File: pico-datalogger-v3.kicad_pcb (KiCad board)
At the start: 2 copper layers, 130 x 65 mm, 60 parts, among them IC1 LM66200DRLR, J1 JST-PH2 Bat, J11 Conn_I2C1, J12 Conn_UART_5V, J13 THT_I2C1, J14 THT_I2C0, J17 Disp_THT, J2 Conn_Pico_Left, J3 Conn_Pico_Right, J4 SM06B-GHS-TB_LF_SN, J6 Conn_Display, J9 Conn_I2C0, Q1 AO3401A, Q2 AO3401A, SW1 SW_Push, SW2 SW_Push, SW3 SW_Push, SW4 SW_Push, SW5 SW_Push, U1 74LVC2G74, U2 PCF8523T, U4 XTSD, U5 SCD40_Breakout, U6 AHT20, U7 RFM95W-868S2, Y1 Crystal

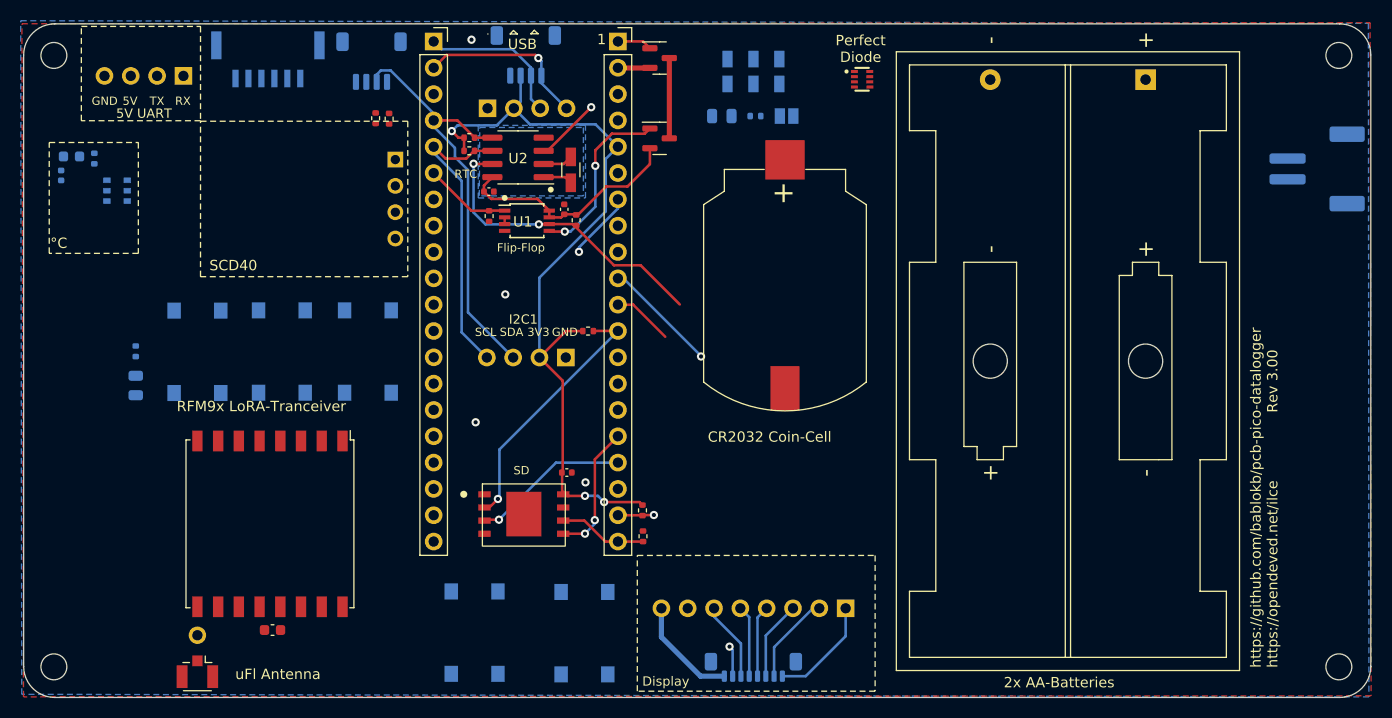
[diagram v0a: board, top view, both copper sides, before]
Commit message: move AA-holder away from mounting-hole
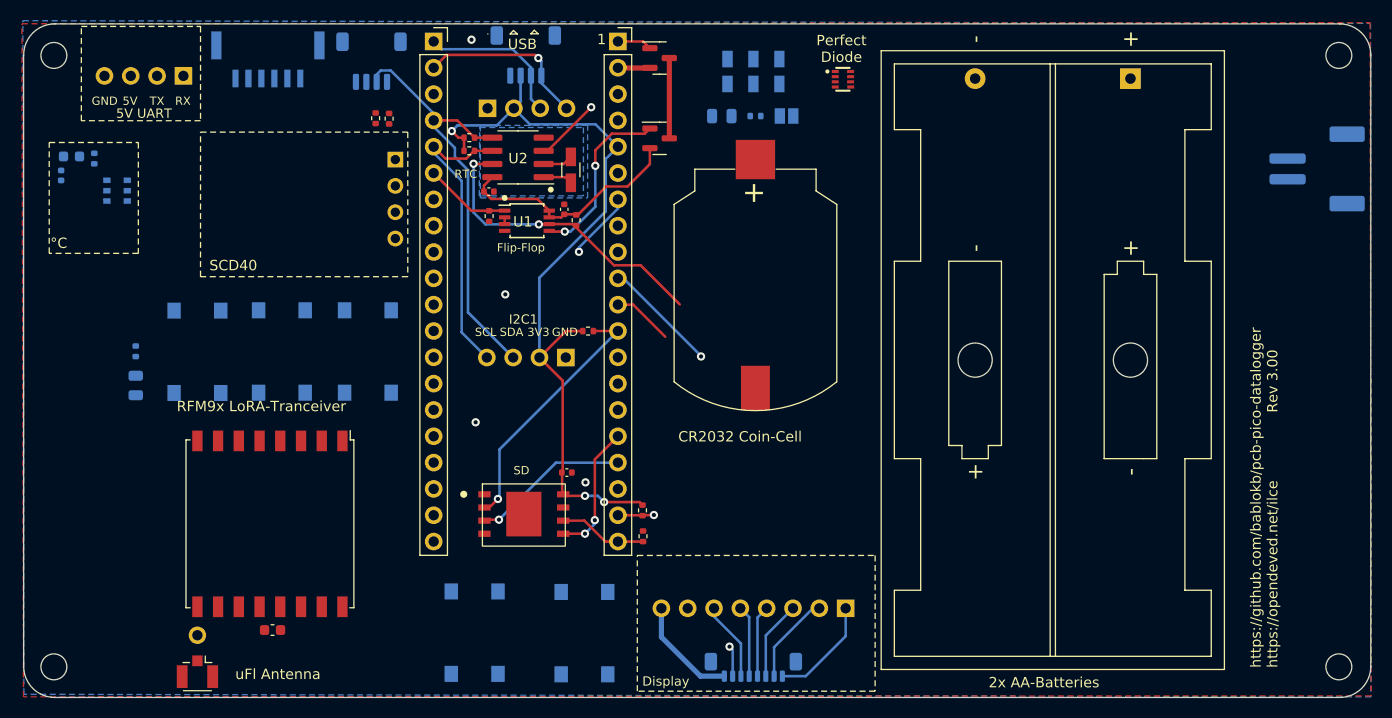
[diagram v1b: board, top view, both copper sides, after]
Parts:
- moved BT1 2.85 mm to (170.7, 124.1)
- moved G*** 2.37 mm to (197.1, 136.0)
- moved IC1 1.85 mm to (179.1, 105.3)
- moved BT2 1.46 mm to (206.9, 105.2)
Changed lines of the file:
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@@
   )
   (footprint "user:LM66200DRLR" (layer "F.Cu")
-    (at 180.99 105.3 -90)
+    (at 179.14 105.3 -90)
     (descr "LM66200DRLR Perfect Diode")
     (property "Description" "1.6-V to 5.5-V, 40-mΩ, 2.5-A, low-IQ, dual ideal diode")
@@
   )
   (footprint "Battery:BatteryHolder_Keystone_2462_2xAA" (layer "F.Cu")
-    (at 208.35 105.335 -90)
+    (at 206.89 105.235 -90)
     (descr "2xAA cell battery holder, Keystone P/N 2462, https://www.keyelco.com/product-pdf.cfm?p=1027")
     (tags "AA battery cell holder")
@@
   )
   (footprint "user:CR2032_Holder" (layer "F.Cu")
-    (at 173.55 124.1 90)
+    (at 170.7 124.075 90)
     (descr "Coin-Cell CR2032")
     (property "LCSC" "C964777")
@@
   )
   (footprint "user:giraffe" locked (layer "B.Cu")
-    (at 199.45 136 180)
+    (at 197.082707 135.960722 180)
     (attr board_only exclude_from_pos_files exclude_from_bom)
     (fp_text reference "G***" (at 0 0) (layer "B.SilkS")
@@
     )
   )
-  (gr_rect (start 105.65 109.3) (end 117.15 100.2)
+  (gr_rect (start 105.65 100.2) (end 117.15 109.3)
     (stroke (width 0.12) (type dash)) (fill none) (layer "B.SilkS"))
   (gr_rect (start 102.55 111.4) (end 111.15 122.05)
@@
   (gr_rect (start 165.105 100.4) (end 175.955 112.05)
     (stroke (width 0.12) (type default)) (fill none) (layer "B.SilkS"))
-  (gr_rect (start 184.15 102.4) (end 217.65 162.45)
+  (gr_rect (start 182.8 102.325) (end 216.3 162.375)
     (stroke (width 0.2) (type dash)) (fill none) (layer "B.SilkS"))
-  (gr_rect (start 158.85 150.75) (end 182.8 164.35)
+  (gr_rect (start 158.85 150.75) (end 182.3 164.35)
     (stroke (width 0.12) (type solid)) (fill none) (layer "B.SilkS"))
   (gr_rect (start 105.65 100.2) (end 117.15 109.3)
@@
   (gr_line (start 147.02 100.93) (end 147.35 100.59)
     (stroke (width 0.12) (type solid)) (layer "F.SilkS"))
-  (gr_rect (start 117.15 109.35) (end 137.15 124.35)
+  (gr_rect (start 117.15 110.4) (end 137.15 124.35)
     (stroke (width 0.12) (type dash)) (fill none) (layer "F.SilkS"))
   (gr_line (start 144.89 100.93) (end 144.87 100.93)
@@
     (effects (font (size 1 1) (thickness 0.15)) (justify left bottom mirror))
   )
-  (gr_text "Display" (at 180.25 163.4) (layer "B.SilkS")
+  (gr_text "Display" (at 179.65 163.35) (layer "B.SilkS")
     (effects (font (size 0.9 0.9) (thickness 0.15)) (justify mirror))
   )
@@
     (effects (font (size 0.8 0.8) (thickness 0.15)) (justify mirror))
   )
-  (gr_text "2x AA-Batteries" (at 207 161.2) (layer "B.SilkS")
+  (gr_text "2x AA-Batteries" (at 205.59143 161.2) (layer "B.SilkS")
     (effects (font (size 1 1) (thickness 0.15)) (justify left bottom mirror))
   )
@@
     (effects (font (size 0.8 0.8) (thickness 0.15)))
   )
-  (gr_text "Perfect\nDiode" (at 180.85 103.75) (layer "F.SilkS")
+  (gr_text "Perfect\nDiode" (at 179 103.75) (layer "F.SilkS")
     (effects (font (size 1 1) (thickness 0.15)) (justify bottom))
   )
@@
     (effects (font (size 0.9 0.9) (thickness 0.15)))
   )
-  (gr_text "2x AA-Batteries" (at 194.658571 164.1) (layer "F.SilkS")
+  (gr_text "2x AA-Batteries" (at 193.198571 164.1) (layer "F.SilkS")
     (effects (font (size 1 1) (thickness 0.15)) (justify left bottom))
   )
@@
     (effects (font (size 0.8 0.8) (thickness 0.15)) (justify left))
   )
-  (gr_text "CR2032 Coin-Cell" (at 166.1 140.4) (layer "F.SilkS")
+  (gr_text "CR2032 Coin-Cell" (at 163.25 140.375) (layer "F.SilkS")
     (effects (font (size 1 1) (thickness 0.15)) (justify left bottom))
   )
@@
     (polygon
       (pts
-        (xy 229.9 164.9)
-        (xy 99.9 164.65)
-        (xy 99.8 99.65)
-        (xy 229.85 99.9)
+        (xy 230.103384 164.899841)
+        (xy 100.103384 164.649841)
+        (xy 100.003384 99.649841)
+        (xy 230.053384 99.899841)
       )
     )
     (polygon
       (pts
-        (xy 143.95 109.75)
-        (xy 143.95 116.75)
-        (xy 154.3 116.75)
-        (xy 154.3 109.75)
+        (xy 144.153384 109.749841)
+        (xy 144.153384 116.749841)
+        (xy 154.503384 116.749841)
+        (xy 154.503384 109.749841)
       )
     )

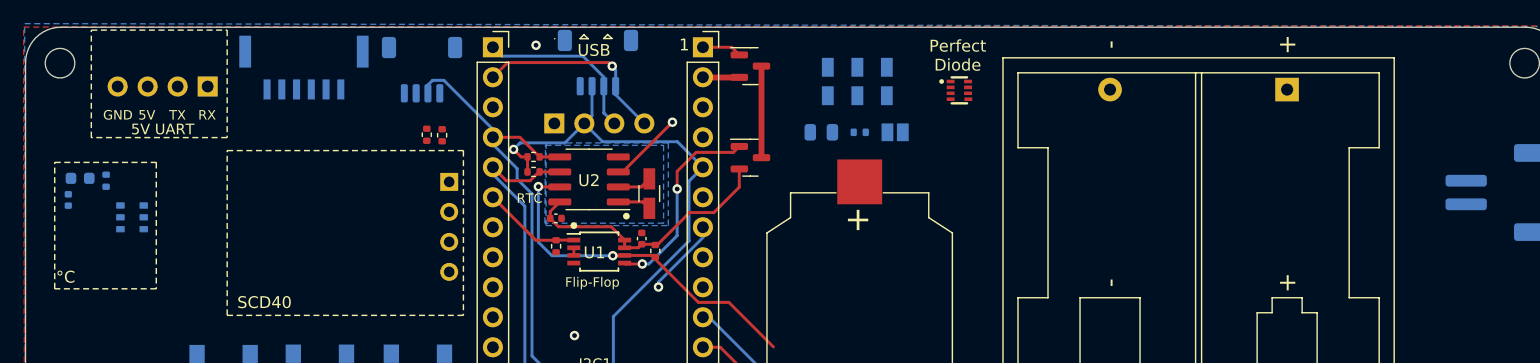
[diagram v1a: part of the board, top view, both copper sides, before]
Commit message: initial routing of power and I2C-devices
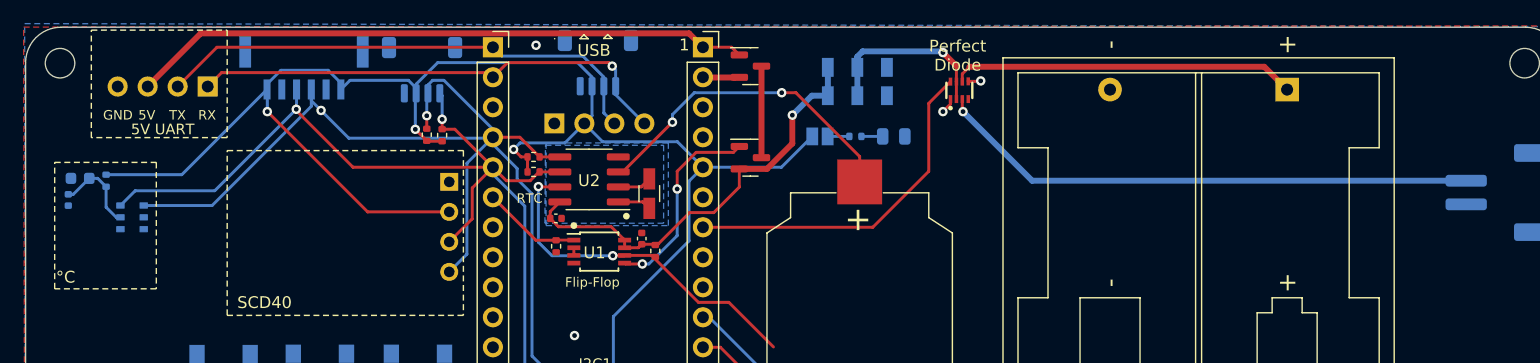
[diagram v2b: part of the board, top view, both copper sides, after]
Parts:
- moved JP1 6.38 mm to (167.3, 109.2), turned to 0 degrees
- moved D1 6.14 mm to (173.6, 109.2)
- moved R11 0.51 mm to (170.3, 109.2), turned to 0 degrees
- turned IC1 to 0 degrees
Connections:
- IC1 pad 8: unconnected-(IC1-ST-Pad8) -> /PS_STATUS
- J3 pad 7: /PDM_DAT -> /PS_STATUS
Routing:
- net +3V3: track 85.9 -> 172.7 mm, vias 3 -> 5
- net SCL: track 28.9 -> 84.2 mm, vias 0 -> 2
- net SDA: track 41.2 -> 93.9 mm, vias 0 -> 2
- net /VBUS: track 3.35 -> 52.7 mm
- net Net-(IC1-VIN1): track 0.00 -> 46.1 mm, vias 0 -> 1
- net /PS_STATUS: track 0.00 -> 29.4 mm
- net Net-(BT2-+): track 0.00 -> 29.2 mm
- net /TX: track 14.7 -> 42.8 mm
- net /RX: track 16.7 -> 41.5 mm
- net Net-(BT1-+): track 6.33 -> 28.0 mm, vias 1 -> 2
- net /VOUT: track 0.00 -> 15.2 mm, vias 0 -> 1
- net +BATT: track 22.8 -> 36.7 mm, vias 0 -> 1
- net Net-(U6-VDD): track 0.00 -> 7.35 mm
- net /PDM_DAT: track 6.62 -> 0.00 mm, vias 1 -> 0
- net GND: track 2.97 -> 5.38 mm, vias 5 -> 7
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
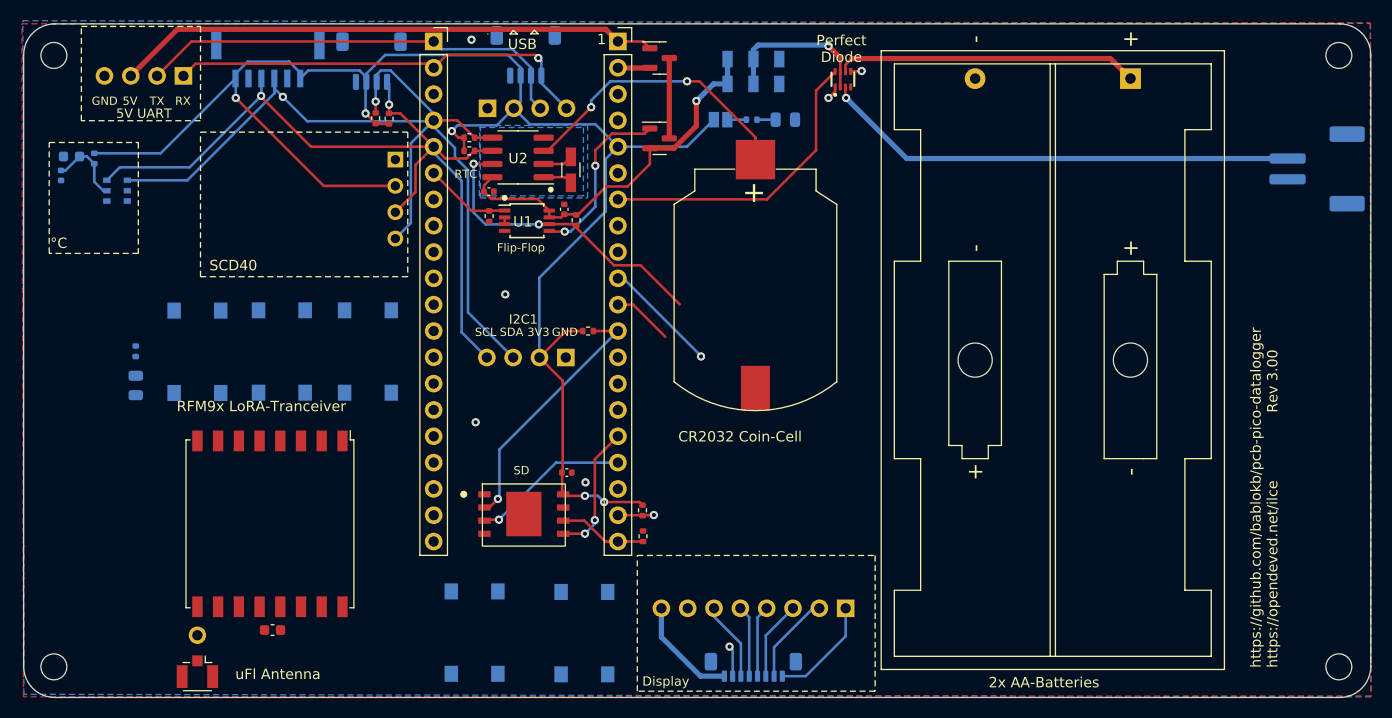
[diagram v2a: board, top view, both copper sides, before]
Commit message: initial routing display-connector, on/rst buttons
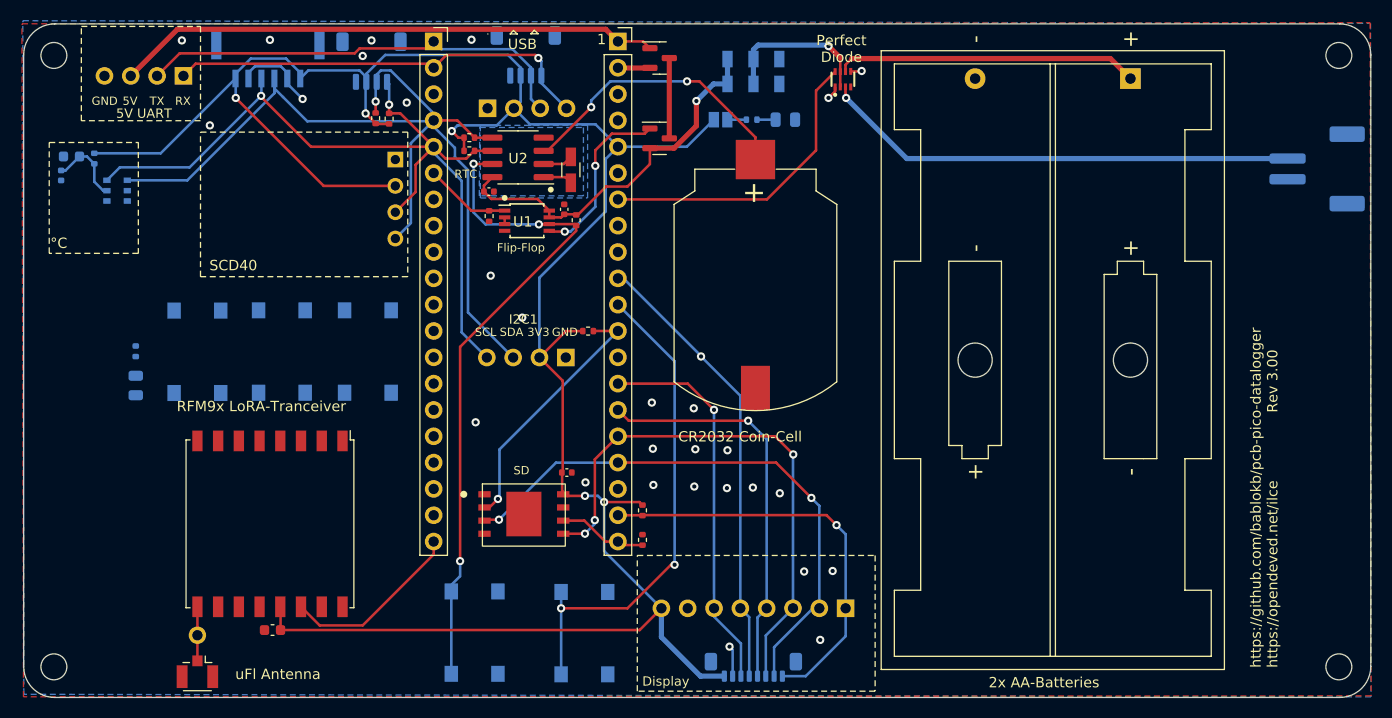
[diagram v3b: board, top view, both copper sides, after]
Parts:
- moved R6 0.35 mm to (159.8, 149.8)
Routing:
- net +3V3: track 172.7 -> 225.4 mm
- net RUN: track 5.85 -> 48.0 mm, vias 0 -> 2
- net ~{ON}: track 30.1 -> 65.2 mm, vias 2 -> 3
- net /MOSI0: track 20.3 -> 52.8 mm, vias 2 -> 3
- net /Display_DC: track 6.92 -> 38.8 mm, vias 0 -> 1
- net /SCLK0: track 24.1 -> 55.2 mm, vias 1 -> 2
- net /Display_RST: track 7.62 -> 37.1 mm, vias 0 -> 1
- net /Display_CS: track 13.9 -> 40.3 mm
- net /Display_BUSY: track 18.1 -> 43.9 mm
- net Lora_DIO0: track 0.00 -> 17.6 mm
- net GND: track 5.38 -> 13.3 mm, vias 7 -> 28
- net /LoRa/ANT: track 0.00 -> 5.22 mm
- net SDA: vias 2 -> 1

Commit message: swapped SWA/SWB with LoRa-RST/LoRa-CS; initial routing of LoRa and buttons
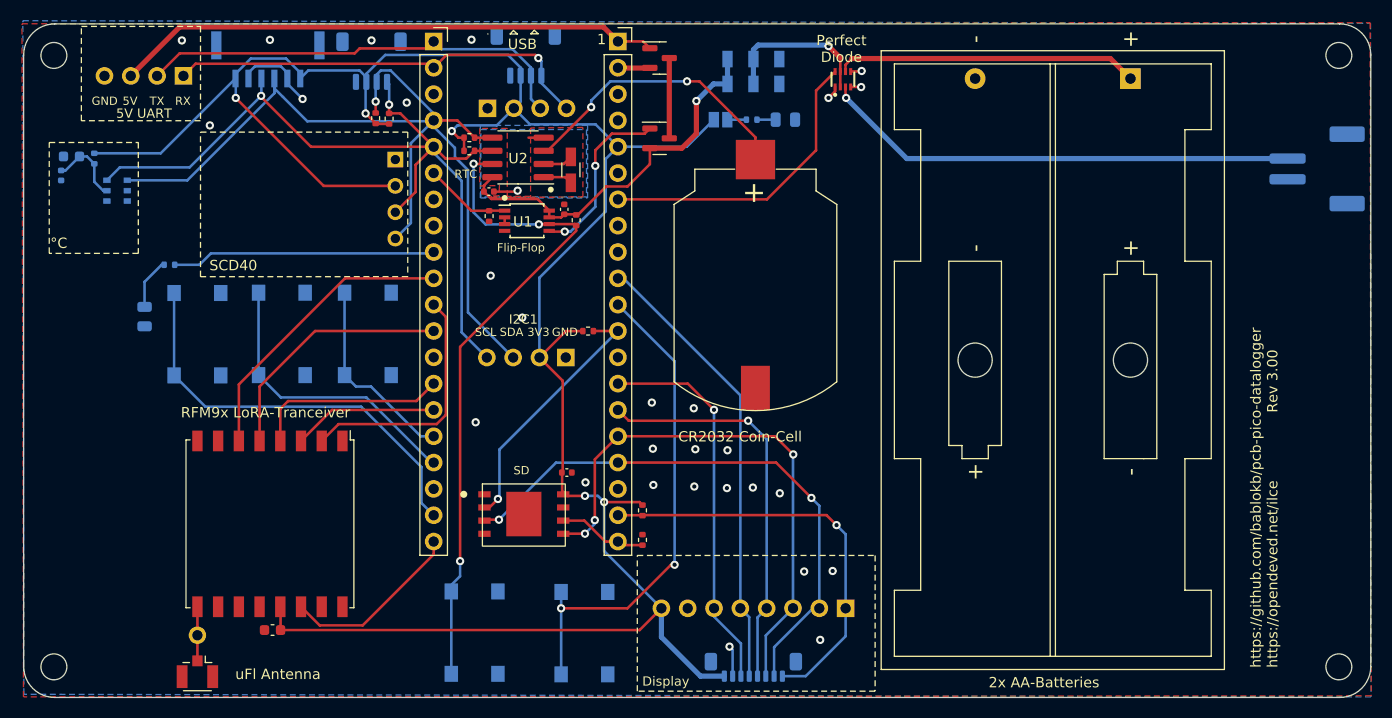
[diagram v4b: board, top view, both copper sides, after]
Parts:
- Y1: footprint Crystal:Crystal_SMD_3215-2Pin_3.2x1.5mm -> user:Crystal_SMD_3215-2Pin_3.2x1.5mm
- moved R12 8.96 mm to (114.2, 123.2), turned to 0 degrees
- moved D2 6.70 mm to (111.8, 128.2)
- moved SW1 1.70 mm to (133.3, 129.9)
- moved SW2 1.70 mm to (125.0, 129.9)
- moved SW3 1.70 mm to (116.8, 129.9)
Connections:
- J2 pad 10: SWA -> Lora_RST
- J2 pad 12: SWB -> Lora_CS
- J2 pad 16: Lora_RST -> SWA
- J2 pad 17: Lora_CS -> SWB
- J2 pad 7: /PDM_CLK -> unconnected-(J2-Pin_7-Pad7)
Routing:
- net SWC: track 0.00 -> 40.6 mm
- net Lora_RST: track 0.00 -> 28.5 mm
- net SWB: track 0.00 -> 28.3 mm
- net SWD: track 0.00 -> 25.5 mm
- net Lora_CS: track 0.00 -> 24.3 mm
- net MISO1: track 0.00 -> 24.1 mm
- net SWA: track 0.00 -> 19.0 mm
- net SCLK1: track 0.00 -> 18.9 mm
- net MOSI1: track 0.00 -> 14.0 mm
- net Net-(D2-A): track 0.00 -> 4.99 mm
- net GND: track 13.3 -> 18.1 mm, vias 28 -> 29
- net /Display_BUSY: vias 1 -> 0
